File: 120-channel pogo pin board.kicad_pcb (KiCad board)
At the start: 2 copper layers, 75 x 50 mm, 241 parts, among them P1 CONN_1, P10 CONN_1, P100 CONN_1, P101 CONN_1, P102 CONN_1, P103 CONN_1, P104 CONN_1, P105 CONN_1, P106 CONN_1, P107 CONN_1, P108 CONN_1, P109 CONN_1, P11 CONN_1, P110 CONN_1, P111 CONN_1, P112 CONN_1, P113 CONN_1, P114 CONN_1, P115 CONN_1, P116 CONN_1, P117 CONN_1, P118 CONN_1, P119 CONN_1, P12 CONN_1, P120 CONN_1, P121 CONN_1, P13 CONN_1, P14 CONN_1, P15 CONN_1, P16 CONN_1, P17 CONN_1, P18 CONN_1, P19 CONN_1, P2 CONN_1, P20 CONN_1, P21 CONN_1, P22 CONN_1, P23 CONN_1, P24 CONN_1, P25 CONN_1, P26 CONN_1, P27 CONN_1, P28 CONN_1, P29 CONN_1, P3 CONN_1, P30 CONN_1, P31 CONN_1, P32 CONN_1, P33 CONN_1, P34 CONN_1, P35 CONN_1, P36 CONN_1, P37 CONN_1, P38 CONN_1, P39 CONN_1, P4 CONN_1, P40 CONN_1, P41 CONN_1, P42 CONN_1, P43 CONN_1, P44 CONN_1, P45 CONN_1, P46 CONN_1, P47 CONN_1, P48 CONN_1, P49 CONN_1, P5 CONN_1, P50 CONN_1, P51 CONN_1, P52 CONN_1, P53 CONN_1, P54 CONN_1, P55 CONN_1, P56 CONN_1, P57 CONN_1, P58 CONN_1, P59 CONN_1, P6 CONN_1, P60 CONN_1, P61 CONN_1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

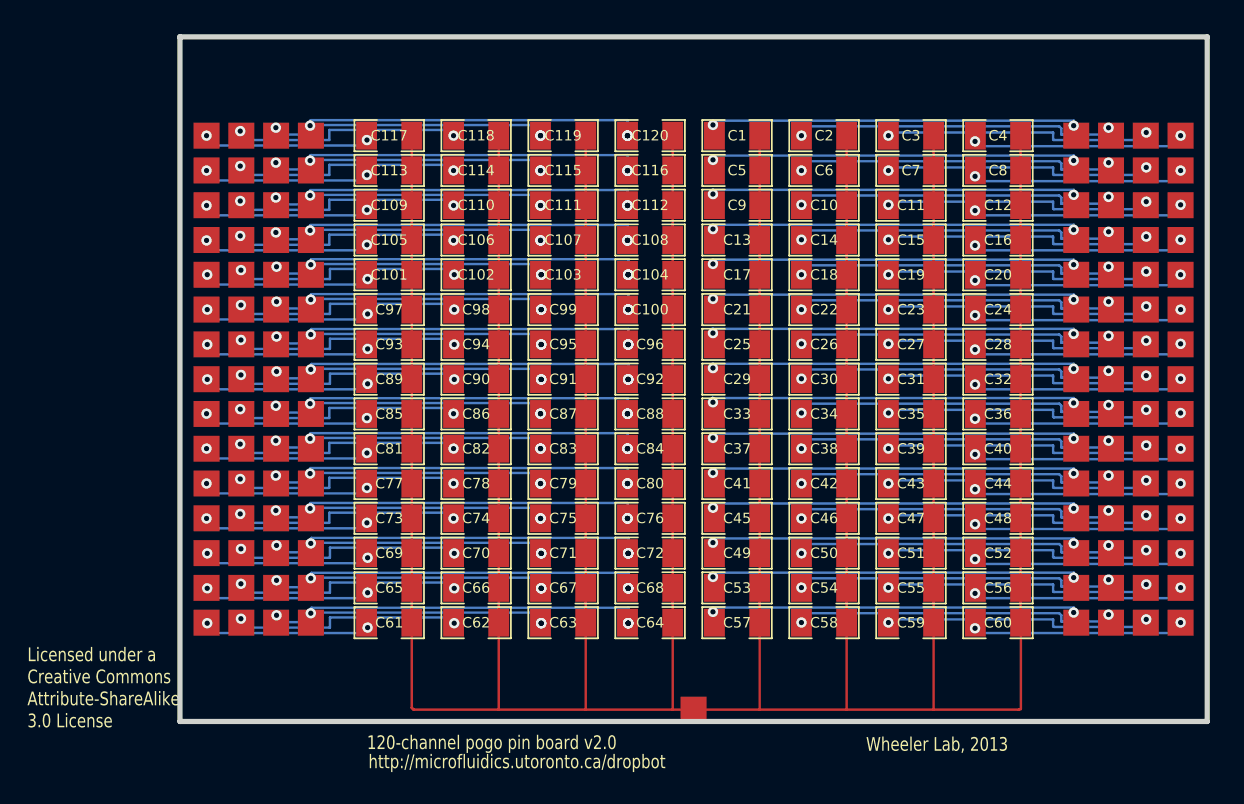
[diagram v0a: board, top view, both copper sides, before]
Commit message: Upgrade to kicad v4.0.0 rc1
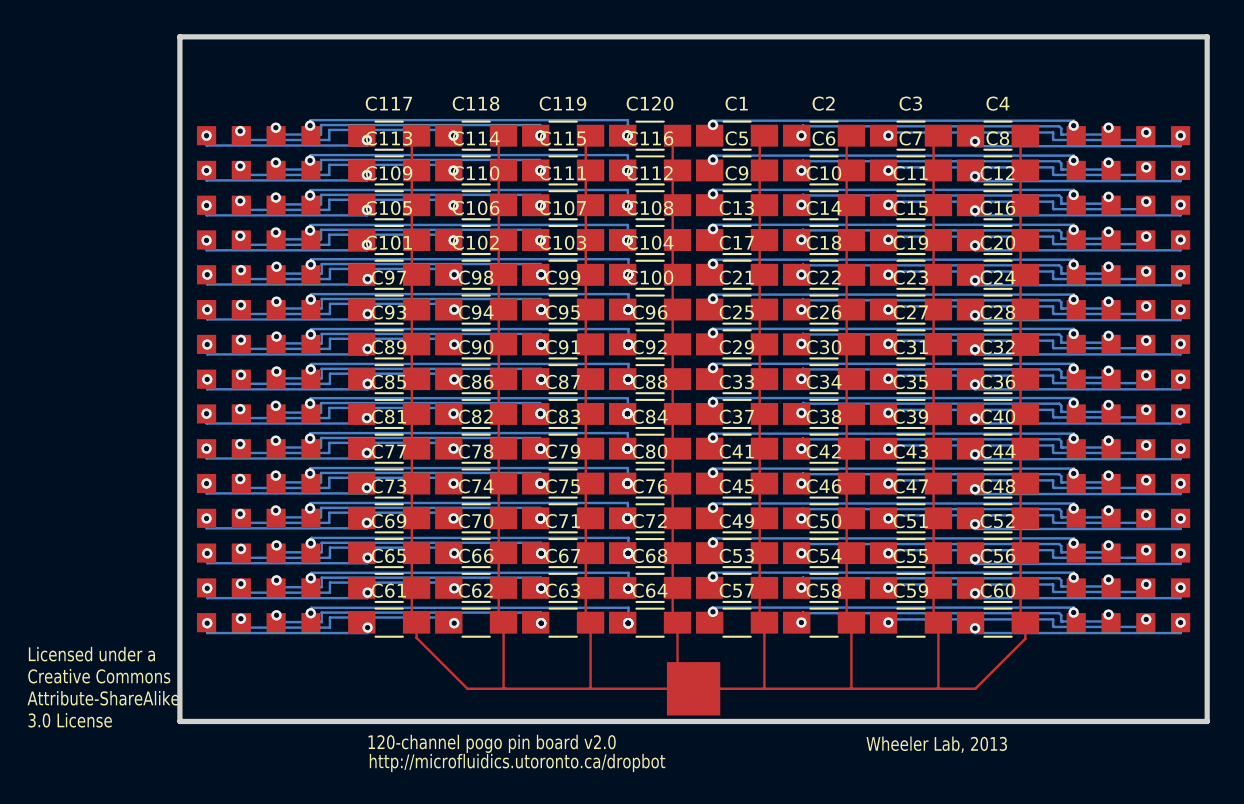
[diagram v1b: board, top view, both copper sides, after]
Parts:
- C1, C10, C100, C101, C102, C103, C104, C105, C106, C107, C108, C109, C11, C110, C111, C112, C113, C114, C115, C116, C117, C118, C119, C12, C120, C13, C14, C15, C16, C17, C18, C19, C2, C20, C21, C22, C23, C24, C25, C26, C27, C28, C29, C3, C30, C31, C32, C33, C34, C35, C36, C37, C38, C39, C4, C40, C41, C42, C43, C44, C45, C46, C47, C48, C49, C5, C50, C51, C52, C53, C54, C55, C56, C57, C58, C59, C6, C60, C61, C62, C63, C64, C65, C66, C67, C68, C69, C7, C70, C71, C72, C73, C74, C75, C76, C77, C78, C79, C8, C80, C81, C82, C83, C84, C85, C86, C87, C88, C89, C9, C90, C91, C92, C93, C94, C95, C96, C97, C98, C99: footprint SM1206 -> Capacitors_SMD:C_1206_HandSoldering
- P1, P10, P100, P101, P102, P103, P104, P105, P106, P107, P108, P109, P11, P110, P111, P112, P113, P114, P115, P116, P117, P118, P119, P12, P120, P13, P14, P15, P16, P17, P18, P19, P2, P20, P21, P22, P23, P24, P25, P26, P27, P28, P29, P3, P30, P31, P32, P33, P34, P35, P36, P37, P38, P39, P4, P40, P41, P42, P43, P44, P45, P46, P47, P48, P49, P5, P50, P51, P52, P53, P54, P55, P56, P57, P58, P59, P6, P60, P61, P62, P63, P64, P65, P66, P67, P68, P69, P7, P70, P71, P72, P73, P74, P75, P76, P77, P78, P79, P8, P80, P81, P82, P83, P84, P85, P86, P87, P88, P89, P9, P90, P91, P92, P93, P94, P95, P96, P97, P98, P99: footprint 1.9mm_DMF_Electrode -> wheelerlab:1.4mm_DMF_Electrode
- P121: footprint 1.9mm_DMF_Electrode -> wheelerlab:3.9mm_DMF_Electrode
- moved P121 1.52 mm to (76.2, 83.6)
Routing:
- net Net-(C1-Pad2): track 380.0 -> 364.4 mm
- net Net-(C1-Pad1): track 27.5 -> 29.2 mm
- net Net-(C33-Pad1): track 27.5 -> 28.4 mm
- net Net-(C25-Pad1): track 27.5 -> 28.4 mm
- net Net-(C29-Pad1): track 27.5 -> 28.4 mm
- net Net-(C9-Pad1): track 27.5 -> 28.4 mm

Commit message: Export gerber files
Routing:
- net Net-(C53-Pad1): track 27.5 -> 28.4 mm
- net Net-(C13-Pad1): track 27.5 -> 28.4 mm
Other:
- board text added: "120-channel test board v1.0-rc0"
- board text added: "Wheeler Lab, 2015"
- board text added: "https://github.com/wheeler-microfluidics/kicad___120-channel_test_board"
- board text removed: "120-channel pogo pin board v2.0"
- board text removed: "Wheeler Lab, 2013"
- board text removed: "http://microfluidics.utoronto.ca/dropbot"
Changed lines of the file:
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@@
   (general
     (links 240)
-    (no_connects 2)
-    (area 38.506399 35.775899 113.893601 86.144101)
+    (no_connects 0)
+    (area 37.692149 35.775899 114.296372 86.144101)
     (thickness 1.6002)
     (drawings 9)
-    (tracks 1425)
+    (tracks 1429)
     (zones 0)
     (modules 241)
@@
     (pad_to_mask_clearance 0.254)
     (aux_axis_origin 0 0)
-    (visible_elements 7FFFFBFF)
+    (visible_elements 7FFFFFFF)
     (pcbplotparams
-      (layerselection 0x00030_80000001)
+      (layerselection 0x010f0_80000001)
       (usegerberextensions true)
       (excludeedgelayer true)
@@
     (add_net "Net-(C99-Pad1)")
   )
+  (module wheelerlab:3.9mm_DMF_Electrode (layer Front)
+    (at 76.2 83.566)
+    (tags "DMF 3.9mm")
+    (clearance 0.0508)
+    (attr smd)
+    (fp_text reference P121 (at -1.22428 -1.39954) (layer F.SilkS) hide
+      (effects (font (size 1.016 0.762) (thickness 0.1524)))
+    )
+    (fp_text value CONN_1 (at 0.0508 1.30048) (layer F.SilkS) hide
+      (effects (font (size 0.762 0.762) (thickness 0.1524)))
+    )
+    (pad 1 thru_hole rect (at 0 0) (size 3.8989 3.8989) (drill 1.016) (layers *.Cu F.SilkS F.Mask)
+      (net 2 "Net-(C1-Pad2)"))
+  )
   (module wheelerlab:1.4mm_DMF_Electrode (layer Front)
     (at 104.14 43.18)
@@
     )
   )
-  (module wheelerlab:3.9mm_DMF_Electrode (layer Front)
-    (at 76.2 83.566)
-    (tags "DMF 3.9mm")
-    (clearance 0.0508)
-    (attr smd)
-    (fp_text reference P121 (at -1.22428 -1.39954) (layer F.SilkS) hide
-      (effects (font (size 1.016 0.762) (thickness 0.1524)))
-    )
-    (fp_text value CONN_1 (at 0.0508 1.30048) (layer F.SilkS) hide
-      (effects (font (size 0.762 0.762) (thickness 0.1524)))
-    )
-    (pad 1 smd rect (at 0 0) (size 3.8989 3.8989) (layers Front F.Mask)
-      (net 2 "Net-(C1-Pad2)"))
-  )
   (gr_line (start 38.6969 35.9664) (end 38.6969 36.0172) (angle 90) (layer Edge.Cuts) (width 0.381))
   (gr_line (start 113.7031 35.9664) (end 38.6969 35.9664) (angle 90) (layer Edge.Cuts) (width 0.381))
@@
   (gr_line (start 38.6969 85.9536) (end 113.7031 85.9536) (angle 90) (layer Edge.Cuts) (width 0.381))
   (gr_line (start 38.6969 35.9664) (end 38.6969 85.9536) (angle 90) (layer Edge.Cuts) (width 0.381))
-  (gr_text http://microfluidics.utoronto.ca/dropbot (at 63.3095 88.9) (layer F.SilkS)
+  (gr_text https://github.com/wheeler-microfluidics/kicad___120-channel_test_board (at 62.738 39.116) (layer F.SilkS)
     (effects (font (size 1 0.8) (thickness 0.2)))
   )
-  (gr_text "Licensed under a\nCreative Commons\nAttribute-ShareAlike\n3.0 License" (at 27.559 83.5025) (layer F.SilkS)
-    (effects (font (size 1 0.8) (thickness 0.2)) (justify left))
+  (gr_text "Licensed under a\nCreative Commons\nAttribute-ShareAlike\n3.0 License" (at 39.624 82.804) (layer F.SilkS)
+    (effects (font (size 0.8 0.6) (thickness 0.15)) (justify left))
   )
-  (gr_text "Wheeler Lab, 2013" (at 93.98 87.63) (layer F.SilkS)
+  (gr_text "Wheeler Lab, 2015" (at 106.426 38.608) (layer F.SilkS)
     (effects (font (size 1 0.8) (thickness 0.2)))
   )
-  (gr_text "120-channel pogo pin board v2.0" (at 61.468 87.503) (layer F.SilkS)
+  (gr_text "120-channel test board v1.0-rc0" (at 50.038 37.592) (layer F.SilkS)
     (effects (font (size 1 0.8) (thickness 0.2)))
   )
@@
   (segment (start 111.75 48.24) (end 111.75 49) (width 0.1778) (layer Back) (net 13))
   (segment (start 111.75 48.24) (end 111.76 48.23) (width 0.1778) (layer Back) (net 13))
+  (segment (start 77.375 50.8) (end 77.375 50.2373) (width 0.1778) (layer Front) (net 14))
+  (segment (start 77.375 50.2373) (end 77.61478 49.99752) (width 0.1778) (layer Front) (net 14))
   (segment (start 77.56578 49.94852) (end 77.61478 49.99752) (width 0.1778) (layer Back) (net 14))
   (segment (start 77.56578 49.94852) (end 77.59118 49.6628) (width 0.1778) (layer Back) (net 14))
@@
   (segment (start 96.774 55.88) (end 96.774 56.276) (width 0.1778) (layer Front) (net 25))
   (via (at 111.76 55.88) (size 0.762) (layers Front Back) (net 25))
-  (segment (start 77.375 58.42) (end 77.375 57.8373) (width 0.1778) (layer Front) (net 26) (status C00000))
-  (segment (start 77.375 57.8373) (end 77.61478 57.59752) (width 0.1778) (layer Front) (net 26) (status 400000))
+  (segment (start 77.375 58.42) (end 77.375 57.8373) (width 0.1778) (layer Front) (net 26))
+  (segment (start 77.375 57.8373) (end 77.61478 57.59752) (width 0.1778) (layer Front) (net 26))
   (segment (start 77.56578 57.54852) (end 77.61478 57.59752) (width 0.1778) (layer Back) (net 26))
   (segment (start 77.56578 57.54852) (end 77.59118 57.2628) (width 0.1778) (layer Back) (net 26))
@@
   (segment (start 96.774 58.38) (end 96.774 58.776) (width 0.1778) (layer Front) (net 29))
   (via (at 111.76 58.38) (size 0.762) (layers Front Back) (net 29))
-  (segment (start 77.375 60.96) (end 77.375 60.3873) (width 0.1778) (layer Front) (net 30) (status C00000))
-  (segment (start 77.375 60.3873) (end 77.61478 60.14752) (width 0.1778) (layer Front) (net 30) (status 400000))
+  (segment (start 77.375 60.96) (end 77.375 60.3873) (width 0.1778) (layer Front) (net 30))
+  (segment (start 77.375 60.3873) (end 77.61478 60.14752) (width 0.1778) (layer Front) (net 30))
   (via (at 77.61478 60.14752) (size 0.762) (layers Front Back) (net 30))
   (segment (start 104.04 60.555) (end 104.04 60.29) (width 0.1778) (layer Front) (net 30))
@@
   (segment (start 111.75 60.94) (end 111.75 61.7) (width 0.1778) (layer Back) (net 33))
   (segment (start 111.75 60.94) (end 111.76 60.93) (width 0.1778) (layer Back) (net 33))
-  (segment (start 77.375 63.5) (end 77.375 62.8873) (width 0.1778) (layer Front) (net 34) (status C00000))
-  (segment (start 77.375 62.8873) (end 77.61478 62.64752) (width 0.1778) (layer Front) (net 34) (status 400000))
+  (segment (start 77.375 63.5) (end 77.375 62.8873) (width 0.1778) (layer Front) (net 34))
+  (segment (start 77.375 62.8873) (end 77.61478 62.64752) (width 0.1778) (layer Front) (net 34))
   (via (at 77.61478 62.64752) (size 0.762) (layers Front Back) (net 34))
   (segment (start 104.04 63.055) (end 104.04 62.79) (width 0.1778) (layer Front) (net 34))
@@
   (segment (start 111.75 73.69) (end 111.75 74.45) (width 0.1778) (layer Back) (net 53))
   (segment (start 111.75 73.69) (end 111.76 73.68) (width 0.1778) (layer Back) (net 53))
+  (segment (start 77.61478 75.96022) (end 77.61478 75.39752) (width 0.1778) (layer Front) (net 54))
+  (segment (start 77.56578 75.34852) (end 77.61478 75.39752) (width 0.1778) (layer Back) (net 54))
+  (segment (start 77.56578 75.34852) (end 77.59118 75.0628) (width 0.1778) (layer Back) (net 54))
+  (segment (start 77.59118 75.0628) (end 77.61618 75.0878) (width 0.1778) (layer Back) (net 54))
+  (segment (start 77.61618 75.0878) (end 103.96618 75.0878) (width 0.1778) (layer Back) (net 54))
+  (segment (start 103.96618 75.0878) (end 103.95 75.45) (width 0.1778) (layer Back) (net 54))
+  (via (at 103.95 75.45) (size 0.762) (layers Front Back) (net 54))
+  (segment (start 103.95 75.45) (end 104.04 75.54) (width 0.1778) (layer Front) (net 54))
   (via (at 77.61478 75.39752) (size 0.762) (layers Front Back) (net 54))
+  (segment (start 77.61478 75.96022) (end 77.375 76.2) (width 0.1778) (layer Front) (net 54))
   (segment (start 104.04 75.805) (end 104.04 75.54) (width 0.1778) (layer Front) (net 54))
-  (segment (start 103.95 75.45) (end 104.04 75.54) (width 0.1778) (layer Front) (net 54))
-  (via (at 103.95 75.45) (size 0.762) (layers Front Back) (net 54))
-  (segment (start 103.96618 75.0878) (end 103.95 75.45) (width 0.1778) (layer Back) (net 54))
-  (segment (start 77.61618 75.0878) (end 103.96618 75.0878) (width 0.1778) (layer Back) (net 54))
-  (segment (start 77.59118 75.0628) (end 77.61618 75.0878) (width 0.1778) (layer Back) (net 54))
-  (segment (start 77.56578 75.34852) (end 77.59118 75.0628) (width 0.1778) (layer Back) (net 54))
-  (segment (start 77.56578 75.34852) (end 77.61478 75.39752) (width 0.1778) (layer Back) (net 54))
   (segment (start 103.15 76.1) (end 106.45 76.1) (width 0.1778) (layer Back) (net 55))
   (segment (start 84.074 76.18) (end 84.2 76.054) (width 0.1778) (layer Back) (net 55))

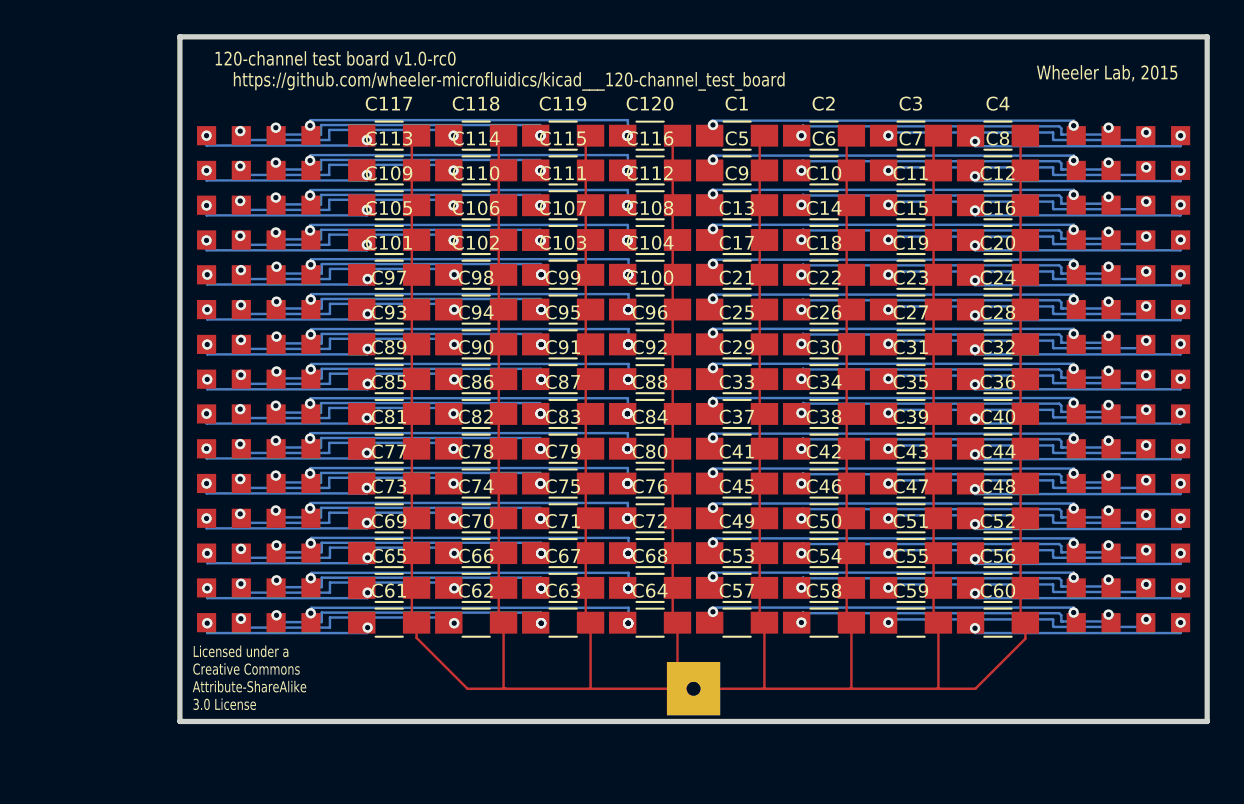
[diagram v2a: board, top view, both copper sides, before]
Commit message: Update for compatibility with DropBot v3
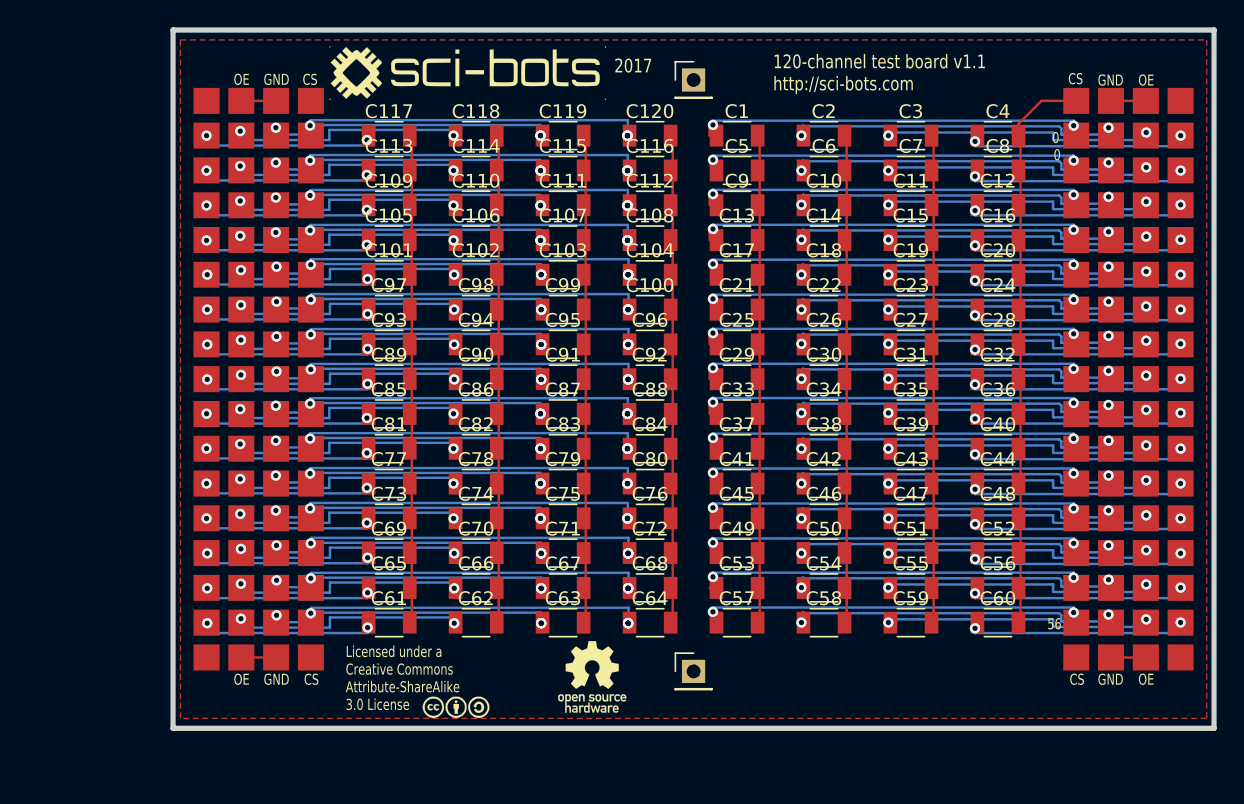
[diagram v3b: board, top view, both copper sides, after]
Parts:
- added G***: LOGO, WheelerLab:SCI-BOTS-LOGO, F.Cu at (59.7, 38.6)
- added G***: LOGO, WheelerLab:CC_S_A_logo_5mm, F.Cu at (58.9, 84.9)
- added G***: LOGO, WheelerLab:OSHW_logo_5mm, F.Cu at (68.8, 82.7)
- added P122: CONN_01X01, wheelerlab:1.9mm_DMF_Electrode, F.Cu at (48.3, 40.6)
- added P123: CONN_01X01, wheelerlab:1.9mm_DMF_Electrode, F.Cu at (48.3, 81.3)
- added P124: CONN_01X01, wheelerlab:1.9mm_DMF_Electrode, F.Cu at (104.1, 81.3)
- added P125: CONN_01X01, wheelerlab:1.9mm_DMF_Electrode, F.Cu at (104.1, 40.6)
- added P126: CONN_01X01, wheelerlab:1.9mm_DMF_Electrode, F.Cu at (45.7, 40.6)
- added P127: CONN_01X01, wheelerlab:1.9mm_DMF_Electrode, F.Cu at (43.2, 40.6)
- added P128: CONN_01X01, wheelerlab:1.9mm_DMF_Electrode, F.Cu at (45.7, 81.3)
- added P129: CONN_01X01, wheelerlab:1.9mm_DMF_Electrode, F.Cu at (43.2, 81.3)
- added P130: CONN_01X01, wheelerlab:1.9mm_DMF_Electrode, F.Cu at (106.7, 81.3)
- added P131: CONN_01X01, wheelerlab:1.9mm_DMF_Electrode, F.Cu at (109.2, 81.3)
- added P132: CONN_01X01, wheelerlab:1.9mm_DMF_Electrode, F.Cu at (106.7, 40.6)
- added P133: CONN_01X01, wheelerlab:1.9mm_DMF_Electrode, F.Cu at (109.2, 40.6)
- added P134: CONN_01X01, wheelerlab:1.9mm_DMF_Electrode, F.Cu at (40.6, 40.6)
- added P135: CONN_01X01, wheelerlab:1.9mm_DMF_Electrode, F.Cu at (40.6, 81.3)
- added P136: CONN_01X01, wheelerlab:1.9mm_DMF_Electrode, F.Cu at (111.8, 81.3)
- added P137: CONN_01X01, wheelerlab:1.9mm_DMF_Electrode, F.Cu at (111.8, 40.6)
- added P138: CONN_01X01, Pin_Headers:Pin_Header_Straight_1x01_Pitch2.54mm, F.Cu at (76.2, 39.1)
- C1, C10, C100, C101, C102, C103, C104, C105, C106, C107, C108, C109, C11, C110, C111, C112, C113, C114, C115, C116, C117, C118, C119, C12, C120, C13, C14, C15, C16, C17, C18, C19, C2, C20, C21, C22, C23, C24, C25, C26, C27, C28, C29, C3, C30, C31, C32, C33, C34, C35, C36, C37, C38, C39, C4, C40, C41, C42, C43, C44, C45, C46, C47, C48, C49, C5, C50, C51, C52, C53, C54, C55, C56, C57, C58, C59, C6, C60, C61, C62, C63, C64, C65, C66, C67, C68, C69, C7, C70, C71, C72, C73, C74, C75, C76, C77, C78, C79, C8, C80, C81, C82, C83, C84, C85, C86, C87, C88, C89, C9, C90, C91, C92, C93, C94, C95, C96, C97, C98, C99: footprint Capacitors_SMD:C_1206_HandSoldering -> Capacitors_SMD:C_1206
- P1, P10, P100, P101, P102, P103, P104, P105, P106, P107, P108, P109, P11, P110, P111, P112, P113, P114, P115, P116, P117, P118, P119, P12, P120, P13, P14, P15, P16, P17, P18, P19, P2, P20, P21, P22, P23, P24, P25, P26, P27, P28, P29, P3, P30, P31, P32, P33, P34, P35, P36, P37, P38, P39, P4, P40, P41, P42, P43, P44, P45, P46, P47, P48, P49, P5, P50, P51, P52, P53, P54, P55, P56, P57, P58, P59, P6, P60, P61, P62, P63, P64, P65, P66, P67, P68, P69, P7, P70, P71, P72, P73, P74, P75, P76, P77, P78, P79, P8, P80, P81, P82, P83, P84, P85, P86, P87, P88, P89, P9, P90, P91, P92, P93, P94, P95, P96, P97, P98, P99: value CONN_1 -> CONN_01X01; footprint wheelerlab:1.4mm_DMF_Electrode -> wheelerlab:1.9mm_DMF_Electrode
- P121: value CONN_1 -> CONN_01X01; footprint wheelerlab:3.9mm_DMF_Electrode -> Pin_Headers:Pin_Header_Straight_1x01_Pitch2.54mm
- moved P121 1.27 mm to (76.2, 82.3)
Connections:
- net Net-(C1-Pad2) renamed CUR_SENSE
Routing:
- net CUR_SENSE: track 364.4 -> 290.3 mm
- net Net-(P128-Pad1): track 0.00 -> 2.54 mm
- net Net-(P126-Pad1): track 0.00 -> 2.54 mm
- net Net-(P132-Pad1): track 0.00 -> 2.54 mm
- net Net-(P130-Pad1): track 0.00 -> 2.54 mm
- added copper zone on F.Cu, net CUR_SENSE
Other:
- board size 75 x 50 mm -> 76 x 51 mm
- board text added: "0"
- board text added: "120-channel test board v1.1 http://sci-bots.com"
- board text added: "2017"
- board text added: "56"
- board text added: "CS"
- board text added: "GND"
- board text added: "OE"
- board text removed: "120-channel test board v1.0-rc0"
- board text removed: "Wheeler Lab, 2015"
- board text removed: "https://github.com/wheeler-microfluidics/kicad___120-channel_test_board"
